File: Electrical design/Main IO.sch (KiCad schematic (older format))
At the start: 98 parts, among them P201 10 A, P202 mA, P203 V R, P204 COMMON, Q201 Q_NMOS_GSD, U201 CT138, U202 MCP6002, U203 MCP6N11, U204 74LVC1G66 GNDA, U205 CT138, U206 74LVC1G66 GNDA, U207 TSV634, U208 74LVC1G66 GNDA, U209 74LVC1G66 GNDA, U210 74LVC1G66 GNDA, U211 74LVC1G66 GNDA, U212 74LVC1G66 GNDA, U213 74LVC1G66 GNDA, U214 74LVC1G66 GNDA, U215 74LVC1G66 GNDA, U216 74LVC1G66 GNDA, U217 74LVC1G66 GNDA, U218 74LVC1G66 GNDA

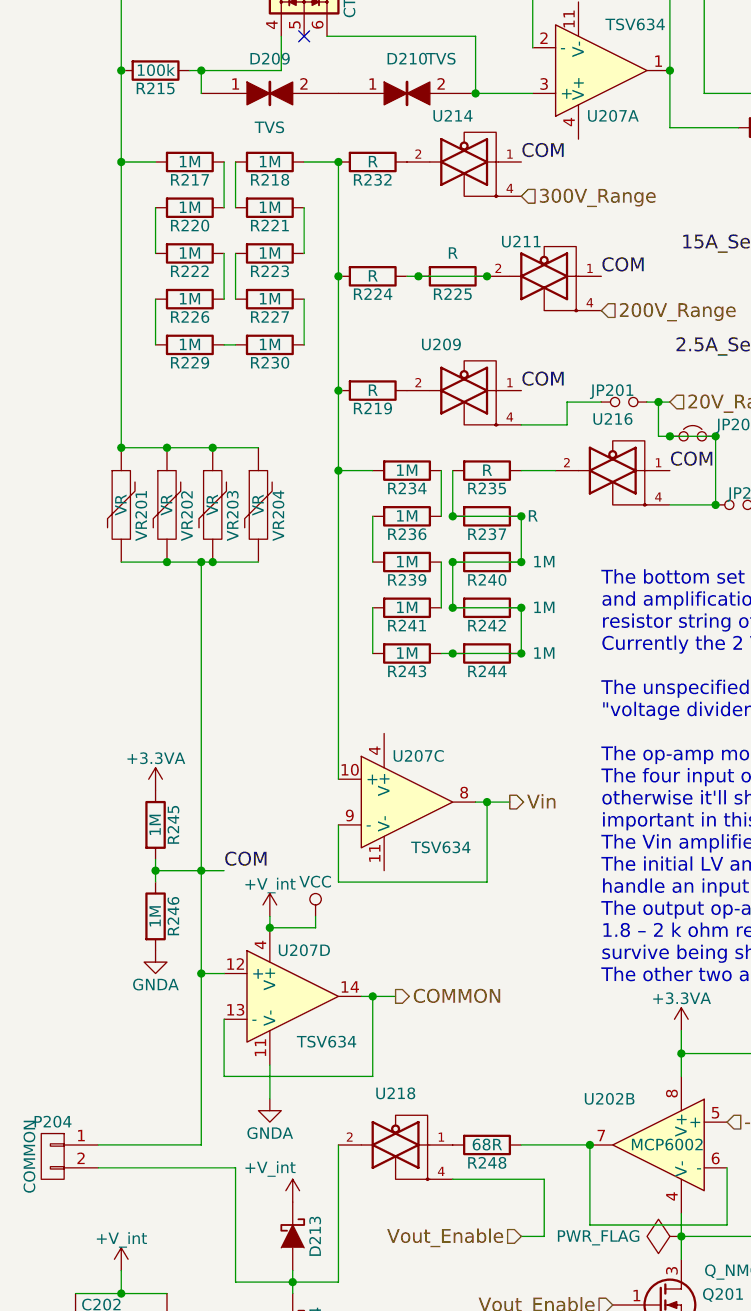
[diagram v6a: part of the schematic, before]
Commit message: Added a resistor in COM to ensure clamping currents are handled correctly.
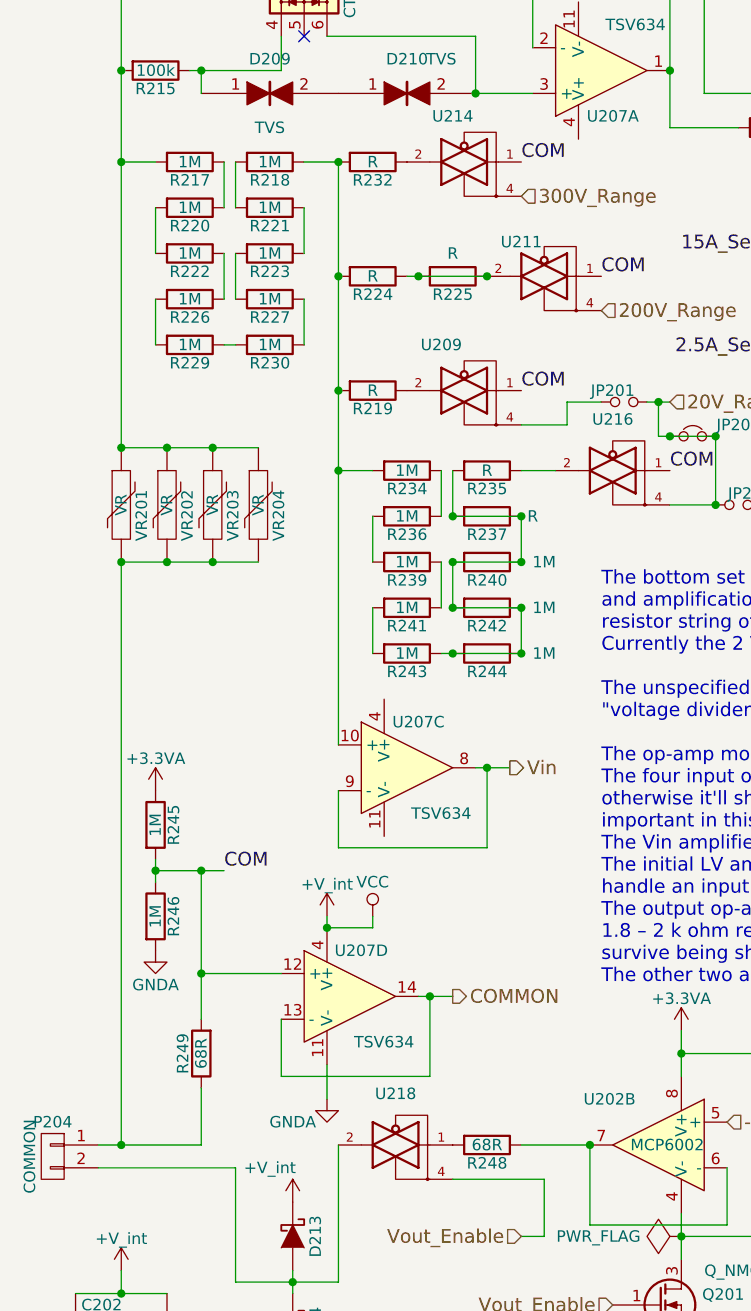
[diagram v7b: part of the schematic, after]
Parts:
- added R249: 68R, my footprints:SMDuniversal_0603to1210_HandSoldering, symbol R
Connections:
- net COM: now also R249.2; no longer P204.1 (P1), VR201.2, VR202.2, VR203.2, VR204.2
- new net: P204.1 (P1), R249.1, VR201.2, VR202.2, VR203.2, VR204.2
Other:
- moved on the sheet: U207C, U207D
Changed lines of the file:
@@
 $EndComp
 NoConn ~ 1800 3050
-Text HLabel 2700 7750 2    60   Output ~ 0
+Text HLabel 2700 7600 2    60   Output ~ 0
 Vin
-Text HLabel 2200 8600 2    60   Output ~ 0
+Text HLabel 2450 8600 2    60   Output ~ 0
 COMMON
 $Comp
@@
 	1300 3300 1400 3300
 Wire Wire Line
-	2550 7750 2700 7750
-Wire Wire Line
-	1950 7850 1950 8100
-Wire Wire Line
-	1950 8100 2600 8100
-Wire Wire Line
-	2600 8100 2600 7750
-Connection ~ 2600 7750
+	2550 7600 2700 7600
+Wire Wire Line
+	1950 7700 1950 7950
+Wire Wire Line
+	1950 7950 2600 7950
+Wire Wire Line
+	2600 7950 2600 7600
+Connection ~ 2600 7600
 Wire Wire Line
 	1000 4950 1150 4950
 Wire Wire Line
-	1350 8500 1450 8500
-Wire Wire Line
-	1450 8700 1450 8950
-Wire Wire Line
-	1450 8950 2100 8950
-Wire Wire Line
-	2100 8950 2100 8600
-Wire Wire Line
-	2050 8600 2200 8600
-Connection ~ 2100 8600
+	1700 8700 1700 8950
+Wire Wire Line
+	1700 8950 2350 8950
+Wire Wire Line
+	2350 8950 2350 8600
+Wire Wire Line
+	2300 8600 2450 8600
+Connection ~ 2350 8600
 Connection ~ 1350 8500
 Wire Wire Line
-	1950 4950 1800 4950
+	1800 4950 1950 4950
 $Comp
 L R R236
@@
 L TLC274 U207
 U 3 1 573720B3
-P 2250 7750
-F 0 "U207" H 2300 7950 50  0000 C CNN
-F 1 "TSV634" H 2400 7550 50  0000 C CNN
-F 2 "my footprints:TSSOP-14_4.4x5mm_Pitch0.65mm" H 2200 7850 50  0001 C CNN
-F 3 "" H 2300 7950 50  0000 C CNN
-	3    2250 7750
+P 2250 7600
+F 0 "U207" H 2300 7800 50  0000 C CNN
+F 1 "TSV634" H 2400 7400 50  0000 C CNN
+F 2 "my footprints:TSSOP-14_4.4x5mm_Pitch0.65mm" H 2200 7700 50  0001 C CNN
+F 3 "" H 2300 7800 50  0000 C CNN
+	3    2250 7600
 	1    0    0    -1
 $EndComp
@@
 L TLC274 U207
 U 4 1 573720BA
-P 1750 8600
-F 0 "U207" H 1800 8800 50  0000 C CNN
-F 1 "TSV634" H 1900 8400 50  0000 C CNN
-F 2 "my footprints:TSSOP-14_4.4x5mm_Pitch0.65mm" H 1700 8700 50  0001 C CNN
-F 3 "" H 1800 8800 50  0000 C CNN
-	4    1750 8600
+P 2000 8600
+F 0 "U207" H 2050 8800 50  0000 C CNN
+F 1 "TSV634" H 2150 8400 50  0000 C CNN
+F 2 "my footprints:TSSOP-14_4.4x5mm_Pitch0.65mm" H 1950 8700 50  0001 C CNN
+F 3 "" H 2050 8800 50  0000 C CNN
+	4    2000 8600
 	1    0    0    -1
 $EndComp
@@
 $EndComp
 Wire Wire Line
-	1950 4950 1950 7650
+	1950 4950 1950 7500
 Wire Wire Line
 	1000 6700 1600 6700
 Connection ~ 1350 8050
-Connection ~ 1350 6700
 Wire Wire Line
 	1000 6200 1600 6200
@@
 COM
 $Comp
-L +V_int #PWR031
+L +V_int #PWR202
 U 1 1 5737B363
 P 4150 2850
-F 0 "#PWR031" H 4150 2700 50  0001 C CNN
+F 0 "#PWR202" H 4150 2700 50  0001 C CNN
 F 1 "+V_int" H 4150 2990 50  0000 C CNN
 F 2 "" H 4150 2850 50  0000 C CNN
@@
 $EndComp
 $Comp
-L VCC #PWR032
+L VCC #PWR210
 U 1 1 5737DBBA
-P 1850 8250
-F 0 "#PWR032" H 1850 8100 50  0001 C CNN
-F 1 "VCC" H 1850 8400 50  0000 C CNN
-F 2 "" H 1850 8250 50  0000 C CNN
-F 3 "" H 1850 8250 50  0000 C CNN
-	1    1850 8250
+P 2100 8250
+F 0 "#PWR210" H 2100 8100 50  0001 C CNN
+F 1 "VCC" H 2100 8400 50  0000 C CNN
+F 2 "" H 2100 8250 50  0000 C CNN
+F 3 "" H 2100 8250 50  0000 C CNN
+	1    2100 8250
 	1    0    0    -1
 $EndComp
@@
 	5500 4000 5400 4000
 $Comp
-L GNDA #PWR033
+L GNDA #PWR211
 U 1 1 573A8247
 P 1150 8400
-F 0 "#PWR033" H 1150 8150 50  0001 C CNN
+F 0 "#PWR211" H 1150 8150 50  0001 C CNN
 F 1 "GNDA" H 1150 8250 50  0000 C CNN
 F 2 "" H 1150 8400 50  0000 C CNN
@@
 $EndComp
 $Comp
-L +3.3VA #PWR034
+L +3.3VA #PWR208
 U 1 1 573A938C
 P 1150 7700
-F 0 "#PWR034" H 1150 7550 50  0001 C CNN
+F 0 "#PWR208" H 1150 7550 50  0001 C CNN
 F 1 "+3.3VA" H 1150 7840 50  0000 C CNN
 F 2 "" H 1150 7700 50  0000 C CNN
@@
 	4000 4800 4100 4800
 $Comp
-L GNDD #PWR035
+L GNDD #PWR206
 U 1 1 573ABBA3
 P 1450 3850
-F 0 "#PWR035" H 1450 3600 50  0001 C CNN
+F 0 "#PWR206" H 1450 3600 50  0001 C CNN
 F 1 "GNDD" H 1450 3700 50  0000 C CNN
 F 2 "" H 1450 3850 50  0000 C CNN
@@
 $EndComp
 $Comp
-L GNDD #PWR036
+L GNDD #PWR201
 U 1 1 573ABD29
 P 1550 2350
-F 0 "#PWR036" H 1550 2100 50  0001 C CNN
+F 0 "#PWR201" H 1550 2100 50  0001 C CNN
 F 1 "GNDD" H 1550 2200 50  0000 C CNN
 F 2 "" H 1550 2350 50  0000 C CNN
@@
 $EndComp
 $Comp
-L +3.3VA #PWR037
+L +3.3VA #PWR203
 U 1 1 573AE254
 P 5700 3600
-F 0 "#PWR037" H 5700 3450 50  0001 C CNN
+F 0 "#PWR203" H 5700 3450 50  0001 C CNN
 F 1 "+3.3VA" H 5700 3740 50  0000 C CNN
 F 2 "" H 5700 3600 50  0000 C CNN
@@
 $EndComp
 $Comp
-L GNDA #PWR038
+L GNDA #PWR207
 U 1 1 573AE493
 P 5700 4400
-F 0 "#PWR038" H 5700 4150 50  0001 C CNN
+F 0 "#PWR207" H 5700 4150 50  0001 C CNN
 F 1 "GNDA" H 5700 4250 50  0000 C CNN
 F 2 "" H 5700 4400 50  0000 C CNN
@@
 $EndComp
 $Comp
-L GNDA #PWR039
+L GNDA #PWR204
 U 1 1 573AE90F
 P 6200 3600
-F 0 "#PWR039" H 6200 3350 50  0001 C CNN
+F 0 "#PWR204" H 6200 3350 50  0001 C CNN
 F 1 "GNDA" H 6200 3450 50  0000 C CNN
 F 2 "" H 6200 3600 50  0000 C CNN
@@
 	5800 4400 5800 4700
 $Comp
-L +V_int #PWR040
+L +V_int #PWR209
 U 1 1 573B1087
-P 1650 8250
-F 0 "#PWR040" H 1650 8100 50  0001 C CNN
-F 1 "+V_int" H 1650 8390 50  0000 C CNN
-F 2 "" H 1650 8250 50  0000 C CNN
-F 3 "" H 1650 8250 50  0000 C CNN
-	1    1650 8250
+P 1900 8250
+F 0 "#PWR209" H 1900 8100 50  0001 C CNN
+F 1 "+V_int" H 1900 8390 50  0000 C CNN
+F 2 "" H 1900 8250 50  0000 C CNN
+F 3 "" H 1900 8250 50  0000 C CNN
+	1    1900 8250
 	1    0    0    -1
 $EndComp
@@
 	1000 4050 1000 6200
 Wire Wire Line
-	1350 6700 1350 9250
-Wire Wire Line
 	1350 9250 900  9250
 Wire Wire Line
@@
 Vout_Enable
 Wire Wire Line
-	1650 9050 1650 8900
-Wire Wire Line
-	1650 8300 1650 8250
+	1900 9050 1900 8900
+Wire Wire Line
+	1900 8300 1900 8250
 $Comp
 L C C202
@@
 Connection ~ 4550 3250
 $Comp
-L GNDA #PWR041
+L GNDA #PWR216
 U 1 1 5758E3FF
 P 3450 10150
-F 0 "#PWR041" H 3450 9900 50  0001 C CNN
+F 0 "#PWR216" H 3450 9900 50  0001 C CNN
 F 1 "GNDA" H 3450 10000 50  0000 C CNN
 F 2 "" H 3450 10150 50  0000 C CNN
@@
 	3450 9550 3450 9750
 $Comp
-L +3.3VA #PWR042
+L +3.3VA #PWR212
 U 1 1 5758E968
 P 3450 8750
-F 0 "#PWR042" H 3450 8600 50  0001 C CNN
+F 0 "#PWR212" H 3450 8600 50  0001 C CNN
 F 1 "+3.3VA" H 3450 8890 50  0000 C CNN
 F 2 "" H 3450 8750 50  0000 C CNN
@@
 $EndComp
 $Comp
-L +V_int #PWR043
+L +V_int #PWR215
 U 1 1 5763C611
 P 1000 9800
-F 0 "#PWR043" H 1000 9650 50  0001 C CNN
+F 0 "#PWR215" H 1000 9650 50  0001 C CNN
 F 1 "+V_int" H 1000 9940 50  0000 C CNN
 F 2 "" H 1000 9800 50  0000 C CNN
@@
 Connection ~ 3450 9650
 $Comp
-L PWR_FLAG #FLG044
+L PWR_FLAG #FLG201
 U 1 1 5767CED2
 P 3450 9650
-F 0 "#FLG044" H 3450 9745 50  0001 C CNN
+F 0 "#FLG201" H 3450 9745 50  0001 C CNN
 F 1 "PWR_FLAG" V 3450 9828 50  0000 L CNN
 F 2 "" H 3450 9650 50  0000 C CNN
@@
 $EndComp
 $Comp
-L +V_int #PWR045
+L +V_int #PWR214
 U 1 1 57834881
 P 1750 9500
-F 0 "#PWR045" H 1750 9350 50  0001 C CNN
+F 0 "#PWR214" H 1750 9350 50  0001 C CNN
 F 1 "+V_int" H 1650 9650 50  0000 C CNN
 F 2 "" H 1750 9500 50  0000 C CNN
@@
 Connection ~ 3600 6150
 $Comp
-L GNDA #PWR046
+L GNDA #PWR217
 U 1 1 578831A0
 P 1750 10200
-F 0 "#PWR046" H 1750 9950 50  0001 C CNN
+F 0 "#PWR217" H 1750 9950 50  0001 C CNN
 F 1 "GNDA" H 1750 10050 50  0000 C CNN
 F 2 "" H 1750 10200 50  0000 C CNN
@@
 $EndComp
 $Comp
-L GNDA #PWR047
+L GNDA #PWR218
 U 1 1 578832E3
 P 1000 10300
-F 0 "#PWR047" H 1000 10050 50  0001 C CNN
+F 0 "#PWR218" H 1000 10050 50  0001 C CNN
 F 1 "GNDA" H 1000 10150 50  0000 C CNN
 F 2 "" H 1000 10300 50  0000 C CNN
@@
 $EndComp
 $Comp
-L GNDA #PWR048
+L GNDA #PWR205
 U 1 1 57883879
 P 4150 3650
-F 0 "#PWR048" H 4150 3400 50  0001 C CNN
+F 0 "#PWR205" H 4150 3400 50  0001 C CNN
 F 1 "GNDA" H 4150 3500 50  0000 C CNN
 F 2 "" H 4150 3650 50  0000 C CNN
@@
 $EndComp
 $Comp
-L GNDA #PWR049
+L GNDA #PWR213
 U 1 1 57884EE1
-P 1650 9050
-F 0 "#PWR049" H 1650 8800 50  0001 C CNN
-F 1 "GNDA" H 1650 8900 50  0000 C CNN
-F 2 "" H 1650 9050 50  0000 C CNN
-F 3 "" H 1650 9050 50  0000 C CNN
-	1    1650 9050
-	1    0    0    -1
-$EndComp
-Wire Wire Line
-	1850 8250 1850 8300
-Wire Wire Line
-	1850 8300 1650 8300
-Connection ~ 1650 8300
+P 1900 9050
+F 0 "#PWR213" H 1900 8800 50  0001 C CNN
+F 1 "GNDA" H 1750 8950 50  0000 C CNN
+F 2 "" H 1900 9050 50  0000 C CNN
+F 3 "" H 1900 9050 50  0000 C CNN
+	1    1900 9050
+	1    0    0    -1
+$EndComp
+Wire Wire Line
+	2100 8250 2100 8300
+Wire Wire Line
+	2100 8300 1900 8300
+Connection ~ 1900 8300
 Wire Wire Line
 	5700 3600 5900 3600
@@
 Wire Wire Line
 	1150 8050 1450 8050
+$Comp
+L R R249
+U 1 1 57871EDB
+P 1350 8850
+F 0 "R249" V 1430 8850 50  0000 C CNN
+F 1 "68R" V 1350 8850 50  0000 C CNN
+F 2 "my footprints:SMDuniversal_0603to1210_HandSoldering" V 1280 8850 50  0001 C CNN
+F 3 "" H 1350 8850 50  0000 C CNN
+	1    1350 8850
+	-1   0    0    1
+$EndComp
+Wire Wire Line
+	1350 8500 1700 8500
+Wire Wire Line
+	1350 9000 1350 9250
+Wire Wire Line
+	1350 8700 1350 8050
+Wire Wire Line
+	1000 9250 1000 6700
+Connection ~ 1000 9250
+Connection ~ 1000 6700
 $EndSCHEMATC

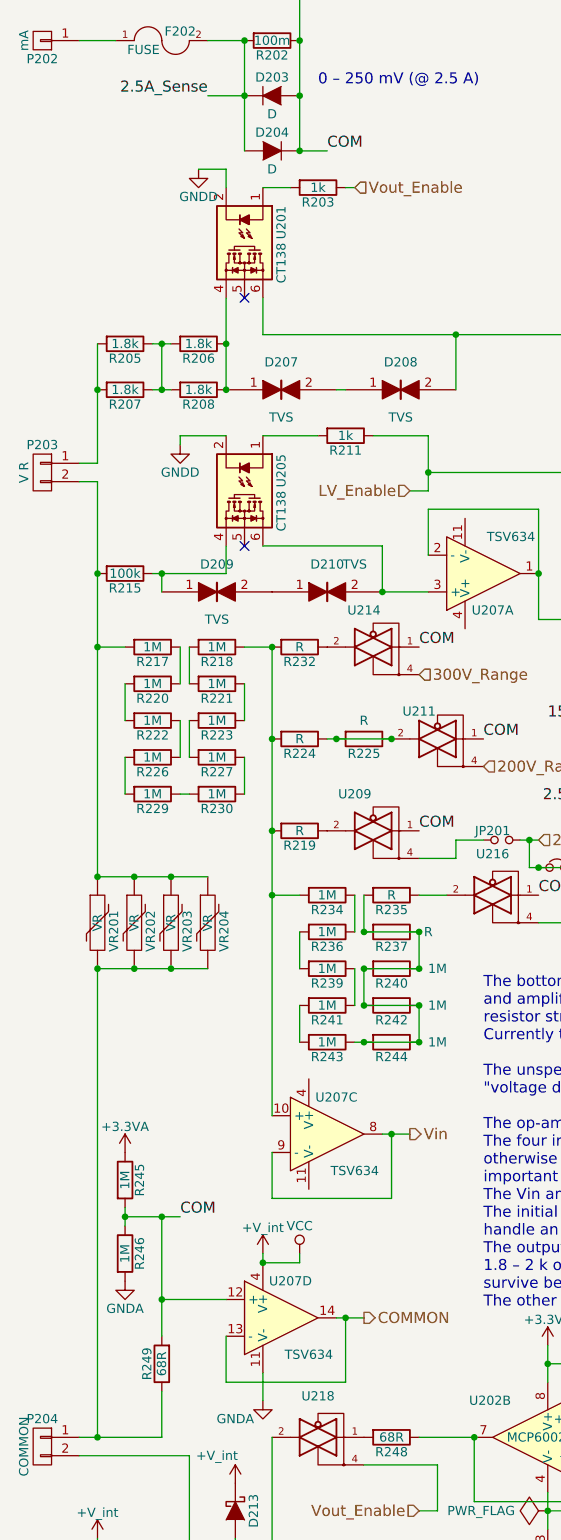
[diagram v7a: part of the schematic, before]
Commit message: Fix current circuit connection, PCB layout.
The current measurement circuit has to connect directly to the Common terminal!
The PCB layout had traces going between the pads of the Common terminal, where
there's actually a non-plated hole. I've updated the footprint to include the hole,
although unfortunately that produces about 20 DRC errors, and also re-routed stuff.
Also updated the value of D301 to match a real Zener diode.
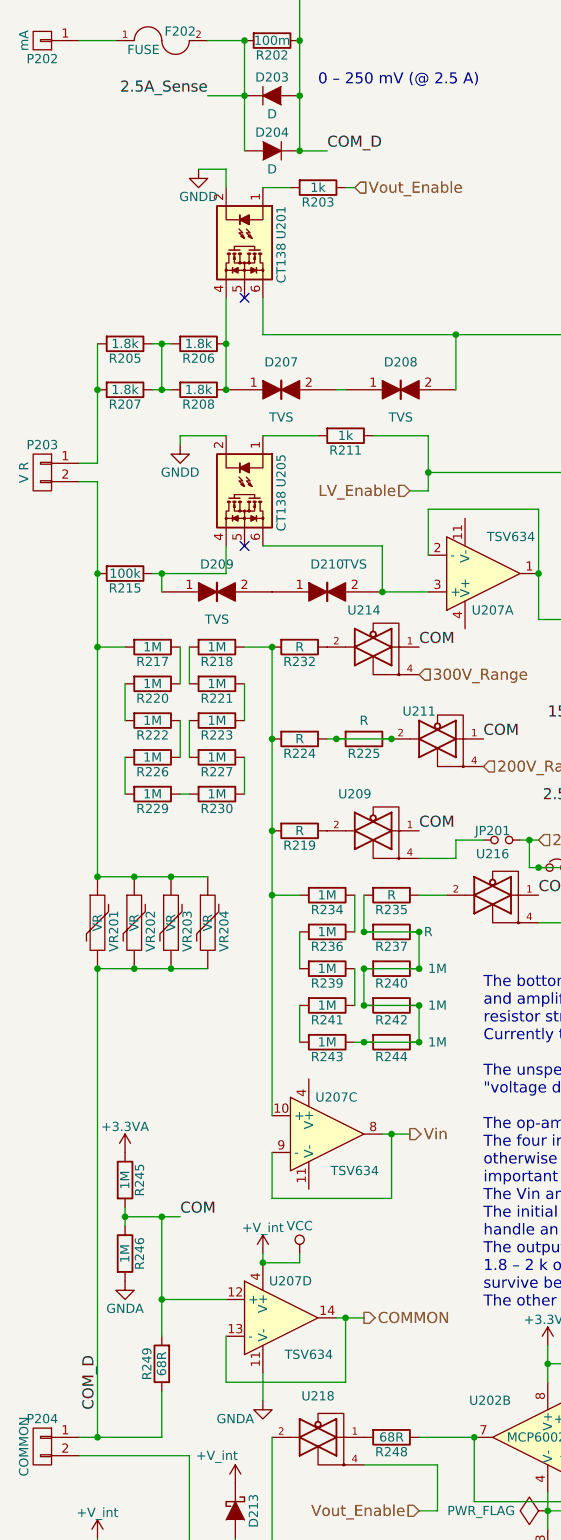
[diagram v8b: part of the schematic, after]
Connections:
- net COM: no longer D201.2 (A), D202.1 (K), D203.2 (A), D204.1 (K), R201.1, R202.1
- net COM_D: now reaches P204.1 (P1), R249.1, VR201.2, VR202.2, VR203.2, VR204.2
- net COM_D: now also D201.2 (A), D202.1 (K), D203.2 (A), D204.1 (K), R201.1, R202.1
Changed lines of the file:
@@
 -Vout
 Text Label 2250 2250 0    60   ~ 0
-COM
+COM_D
 $Comp
 L +V_int #PWR202
@@
 Connection ~ 1000 9250
 Connection ~ 1000 6700
+Text Label 1000 9100 1    60   ~ 0
+COM_D
 $EndSCHEMATC
